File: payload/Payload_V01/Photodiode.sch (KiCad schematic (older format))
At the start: 4 parts

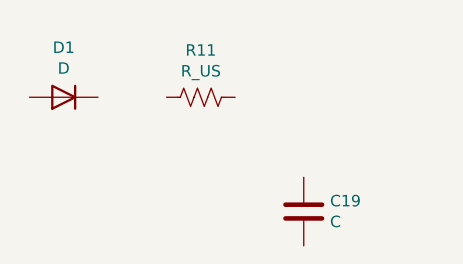
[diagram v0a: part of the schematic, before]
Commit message: added footprints and 3d models
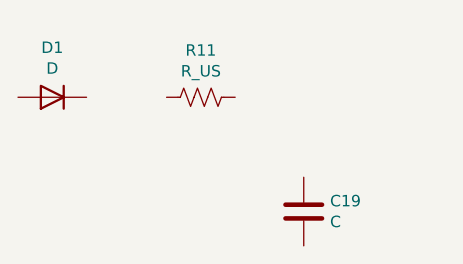
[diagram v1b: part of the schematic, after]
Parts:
- C19, R11: footprint (none) -> Resistor_SMD:R_0603_1608Metric_Pad1.05x0.95mm_HandSolder
- D1: footprint OptoDevice:LaserDiode_TO18-D5.6-3 -> Diode_SMD:D_0603_1608Metric_Pad1.05x0.95mm_HandSolder
- D2: footprint Package_TO_SOT_THT:TO-5-8 -> Package_TO_SOT_THT:TO-5-3
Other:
- moved on the sheet: D1
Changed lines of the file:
@@
 F 0 "D2" H 6850 3245 50  0000 C CNN
 F 1 "D_Photo" H 6850 3154 50  0000 C CNN
-F 2 "Package_TO_SOT_THT:TO-5-8" H 6850 2950 50  0001 C CNN
+F 2 "Package_TO_SOT_THT:TO-5-3" H 6850 2950 50  0001 C CNN
 F 3 "~" H 6850 2950 50  0001 C CNN
 	1    6900 2950
@@
 L Device:D D1
 U 1 1 5F18E7AC
-P 4950 2950
-F 0 "D1" H 4950 2733 50  0000 C CNN
-F 1 "D" H 4950 2824 50  0000 C CNN
-F 2 "OptoDevice:LaserDiode_TO18-D5.6-3" H 4950 2950 50  0001 C CNN
-F 3 "~" H 4950 2950 50  0001 C CNN
-	1    4950 2950
+P 4900 2950
+F 0 "D1" H 4900 2733 50  0000 C CNN
+F 1 "D" H 4900 2824 50  0000 C CNN
+F 2 "Diode_SMD:D_0603_1608Metric_Pad1.05x0.95mm_HandSolder" H 4900 2950 50  0001 C CNN
+F 3 "~" H 4900 2950 50  0001 C CNN
+	1    4900 2950
 	-1   0    0    1
 $EndComp
@@
 F 0 "R11" V 5345 2950 50  0000 C CNN
 F 1 "R_US" V 5436 2950 50  0000 C CNN
-F 2 "" V 5590 2940 50  0001 C CNN
+F 2 "Resistor_SMD:R_0603_1608Metric_Pad1.05x0.95mm_HandSolder" V 5590 2940 50  0001 C CNN
 F 3 "~" H 5550 2950 50  0001 C CNN
 	1    5550 2950
@@
 F 0 "C19" H 6115 3496 50  0000 L CNN
 F 1 "C" H 6115 3405 50  0000 L CNN
-F 2 "" H 6038 3300 50  0001 C CNN
+F 2 "Resistor_SMD:R_0603_1608Metric_Pad1.05x0.95mm_HandSolder" H 6038 3300 50  0001 C CNN
 F 3 "~" H 6000 3450 50  0001 C CNN
 	1    6000 3450

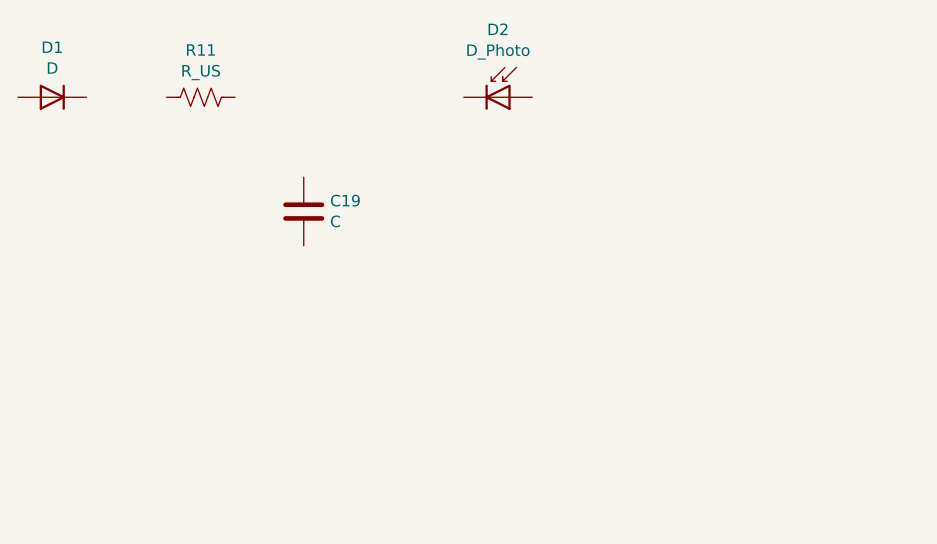
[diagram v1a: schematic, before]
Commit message: created photodiode circuit
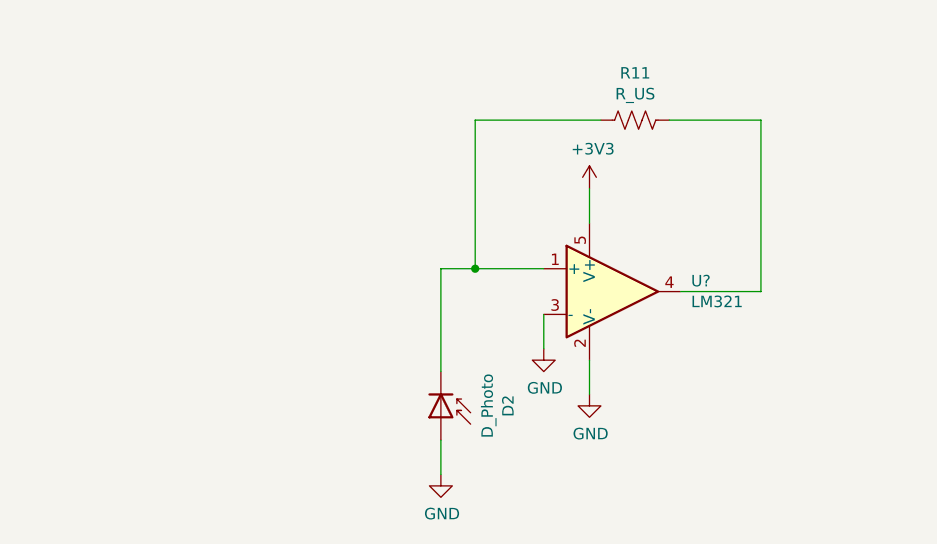
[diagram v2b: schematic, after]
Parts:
- removed C19: C, Resistor_SMD:R_0603_1608Metric_Pad1.05x0.95mm_HandSolder, symbol Device:C
- removed D1: D, Diode_SMD:D_0603_1608Metric_Pad1.05x0.95mm_HandSolder, symbol Device:D
- added U?: LM321, Package_TO_SOT_SMD:SOT-23-5, symbol Amplifier_Operational:LM321
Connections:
- net at D2.1 (K): now also R11.2, U?.1 (+)
- net GND: now reaches D2.2 (A)
- net GND: now also U?.2 (V-), U?.3 (-)
- net at R11.1: now also U?.4
- new net +3V3: U?.5 (V+)
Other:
- moved on the sheet: D2, R11
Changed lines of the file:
@@
 L Device:D_Photo D2
 U 1 1 5F18CDA2
-P 6900 2950
-F 0 "D2" H 6850 3245 50  0000 C CNN
-F 1 "D_Photo" H 6850 3154 50  0000 C CNN
-F 2 "Package_TO_SOT_THT:TO-5-3" H 6850 2950 50  0001 C CNN
-F 3 "~" H 6850 2950 50  0001 C CNN
-	1    6900 2950
-	1    0    0    -1
-$EndComp
-$Comp
-L Device:D D1
-U 1 1 5F18E7AC
-P 4900 2950
-F 0 "D1" H 4900 2733 50  0000 C CNN
-F 1 "D" H 4900 2824 50  0000 C CNN
-F 2 "Diode_SMD:D_0603_1608Metric_Pad1.05x0.95mm_HandSolder" H 4900 2950 50  0001 C CNN
-F 3 "~" H 4900 2950 50  0001 C CNN
-	1    4900 2950
-	-1   0    0    1
+P 6600 4350
+F 0 "D2" H 6550 4645 50  0000 C CNN
+F 1 "D_Photo" H 6550 4554 50  0000 C CNN
+F 2 "Package_TO_SOT_THT:TO-5-3" H 6550 4350 50  0001 C CNN
+F 3 "~" H 6550 4350 50  0001 C CNN
+	1    6600 4350
+	0    1    1    0
 $EndComp
 $Comp
 L Device:R_US R11
 U 1 1 5F18FAFE
-P 5550 2950
-F 0 "R11" V 5345 2950 50  0000 C CNN
-F 1 "R_US" V 5436 2950 50  0000 C CNN
-F 2 "Resistor_SMD:R_0603_1608Metric_Pad1.05x0.95mm_HandSolder" V 5590 2940 50  0001 C CNN
-F 3 "~" H 5550 2950 50  0001 C CNN
-	1    5550 2950
+P 7450 3050
+F 0 "R11" V 7245 3050 50  0000 C CNN
+F 1 "R_US" V 7336 3050 50  0000 C CNN
+F 2 "Resistor_SMD:R_0603_1608Metric_Pad1.05x0.95mm_HandSolder" V 7490 3040 50  0001 C CNN
+F 3 "~" H 7450 3050 50  0001 C CNN
+	1    7450 3050
 	0    1    1    0
 $EndComp
 $Comp
-L Device:C C19
-U 1 1 5F1900F1
-P 6000 3450
-F 0 "C19" H 6115 3496 50  0000 L CNN
-F 1 "C" H 6115 3405 50  0000 L CNN
-F 2 "Resistor_SMD:R_0603_1608Metric_Pad1.05x0.95mm_HandSolder" H 6038 3300 50  0001 C CNN
-F 3 "~" H 6000 3450 50  0001 C CNN
-	1    6000 3450
+L Amplifier_Operational:LM321 U?
+U 1 1 5F2BBB69
+P 7350 3800
+F 0 "U?" H 7694 3846 50  0000 L CNN
+F 1 "LM321" H 7694 3755 50  0000 L CNN
+F 2 "Package_TO_SOT_SMD:SOT-23-5" H 7350 3800 50  0001 C CNN
+F 3 "http://www.ti.com/lit/ds/symlink/lm321.pdf" H 7350 3800 50  0001 C CNN
+	1    7350 3800
 	1    0    0    -1
 $EndComp
+$Comp
+L power:+3V3 #PWR?
+U 1 1 5F2BC2D1
+P 7250 3350
+F 0 "#PWR?" H 7250 3200 50  0001 C CNN
+F 1 "+3V3" H 7265 3523 50  0000 C CNN
+F 2 "" H 7250 3350 50  0001 C CNN
+F 3 "" H 7250 3350 50  0001 C CNN
+	1    7250 3350
+	1    0    0    -1
+$EndComp
+Wire Wire Line
+	7250 3500 7250 3350
+$Comp
+L power:GND #PWR?
+U 1 1 5F2BD2DA
+P 7250 4250
+F 0 "#PWR?" H 7250 4000 50  0001 C CNN
+F 1 "GND" H 7255 4077 50  0000 C CNN
+F 2 "" H 7250 4250 50  0001 C CNN
+F 3 "" H 7250 4250 50  0001 C CNN
+	1    7250 4250
+	1    0    0    -1
+$EndComp
+Wire Wire Line
+	7250 4100 7250 4250
+$Comp
+L power:GND #PWR?
+U 1 1 5F2BDCA6
+P 7050 4050
+F 0 "#PWR?" H 7050 3800 50  0001 C CNN
+F 1 "GND" H 7055 3877 50  0000 C CNN
+F 2 "" H 7050 4050 50  0001 C CNN
+F 3 "" H 7050 4050 50  0001 C CNN
+	1    7050 4050
+	1    0    0    -1
+$EndComp
+Wire Wire Line
+	7050 3900 7050 4050
+Wire Wire Line
+	6750 3700 6750 3050
+Wire Wire Line
+	6750 3050 7300 3050
+Wire Wire Line
+	8000 3050 8000 3800
+Wire Wire Line
+	8000 3800 7650 3800
+Wire Wire Line
+	6600 4150 6600 3700
+Wire Wire Line
+	6600 3700 6750 3700
+Connection ~ 6750 3700
+Wire Wire Line
+	6750 3700 7050 3700
+$Comp
+L power:GND #PWR?
+U 1 1 5F2BF8EA
+P 6600 4600
+F 0 "#PWR?" H 6600 4350 50  0001 C CNN
+F 1 "GND" H 6605 4427 50  0000 C CNN
+F 2 "" H 6600 4600 50  0001 C CNN
+F 3 "" H 6600 4600 50  0001 C CNN
+	1    6600 4600
+	1    0    0    -1
+$EndComp
+Wire Wire Line
+	7600 3050 8000 3050
+Wire Wire Line
+	6600 4450 6600 4600
 $EndSCHEMATC

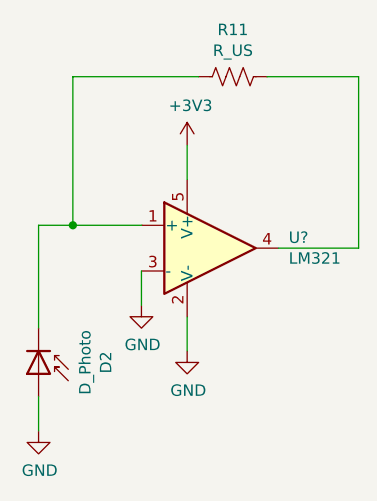
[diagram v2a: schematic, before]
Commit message: fixed op amp footprint
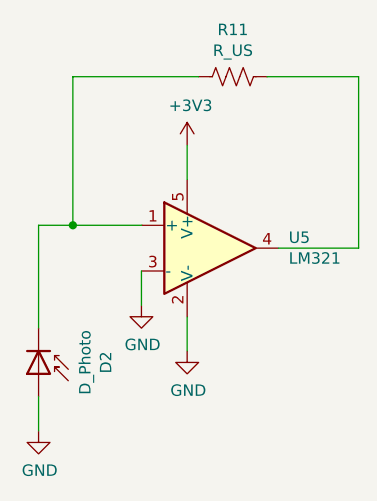
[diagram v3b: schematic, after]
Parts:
- gave numbers to parts that had none: 1
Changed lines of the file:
@@
 $EndComp
 $Comp
-L Amplifier_Operational:LM321 U?
+L Amplifier_Operational:LM321 U5
 U 1 1 5F2BBB69
 P 7350 3800
-F 0 "U?" H 7694 3846 50  0000 L CNN
+F 0 "U5" H 7694 3846 50  0000 L CNN
 F 1 "LM321" H 7694 3755 50  0000 L CNN
 F 2 "Package_TO_SOT_SMD:SOT-23-5" H 7350 3800 50  0001 C CNN
@@
 $EndComp
 $Comp
-L power:+3V3 #PWR?
+L power:+3V3 #PWR0129
 U 1 1 5F2BC2D1
 P 7250 3350
-F 0 "#PWR?" H 7250 3200 50  0001 C CNN
+F 0 "#PWR0129" H 7250 3200 50  0001 C CNN
 F 1 "+3V3" H 7265 3523 50  0000 C CNN
 F 2 "" H 7250 3350 50  0001 C CNN
@@
 	7250 3500 7250 3350
 $Comp
-L power:GND #PWR?
+L power:GND #PWR0130
 U 1 1 5F2BD2DA
 P 7250 4250
-F 0 "#PWR?" H 7250 4000 50  0001 C CNN
+F 0 "#PWR0130" H 7250 4000 50  0001 C CNN
 F 1 "GND" H 7255 4077 50  0000 C CNN
 F 2 "" H 7250 4250 50  0001 C CNN
@@
 	7250 4100 7250 4250
 $Comp
-L power:GND #PWR?
+L power:GND #PWR0131
 U 1 1 5F2BDCA6
 P 7050 4050
-F 0 "#PWR?" H 7050 3800 50  0001 C CNN
+F 0 "#PWR0131" H 7050 3800 50  0001 C CNN
 F 1 "GND" H 7055 3877 50  0000 C CNN
 F 2 "" H 7050 4050 50  0001 C CNN
@@
 	6750 3700 7050 3700
 $Comp
-L power:GND #PWR?
+L power:GND #PWR0132
 U 1 1 5F2BF8EA
 P 6600 4600
-F 0 "#PWR?" H 6600 4350 50  0001 C CNN
+F 0 "#PWR0132" H 6600 4350 50  0001 C CNN
 F 1 "GND" H 6605 4427 50  0000 C CNN
 F 2 "" H 6600 4600 50  0001 C CNN

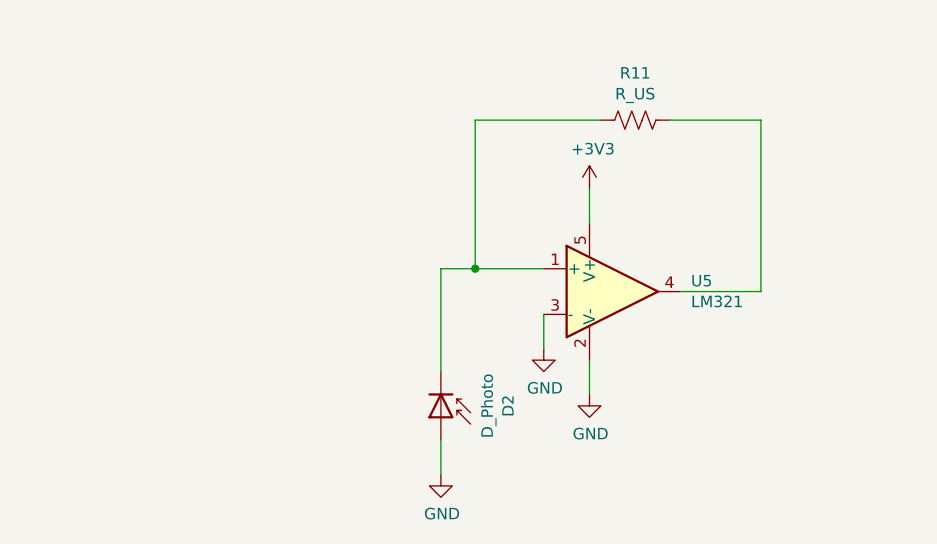
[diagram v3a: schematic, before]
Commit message: added some more pins
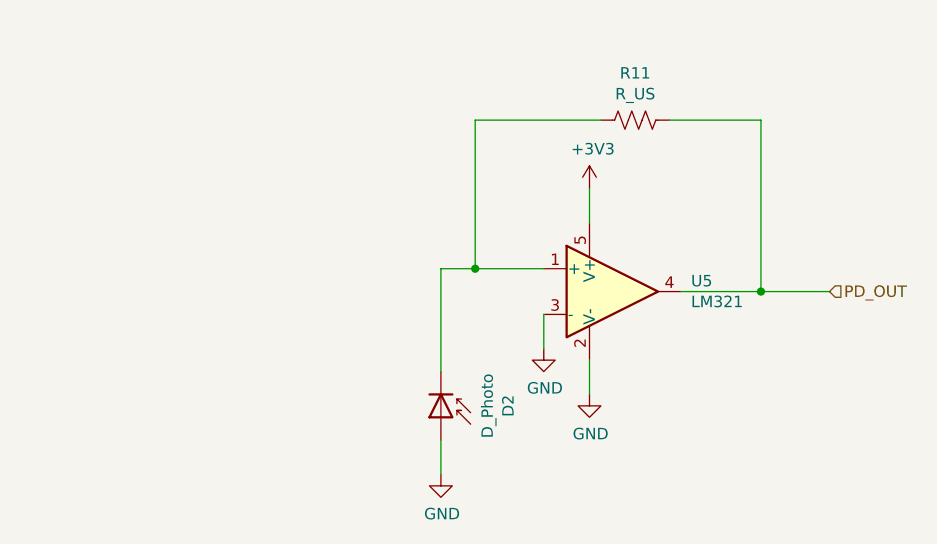
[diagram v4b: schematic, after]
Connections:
- net PD_OUT: now reaches R11.1, U5.4
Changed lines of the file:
@@
 Wire Wire Line
 	6600 4450 6600 4600
+Text HLabel 8300 3800 2    50   Input ~ 0
+PD_OUT
+Wire Wire Line
+	8000 3800 8300 3800
+Connection ~ 8000 3800
 $EndSCHEMATC
